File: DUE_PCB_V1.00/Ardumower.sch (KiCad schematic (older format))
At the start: 54 parts, among them J1 9V IN, J10 Sonar_R, J11 Sonar_C, J12 Sonar_L, J13 P_Right, J14 DS3231 RTC, J15 Button, J16 Button, J17 Button, J18 Button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

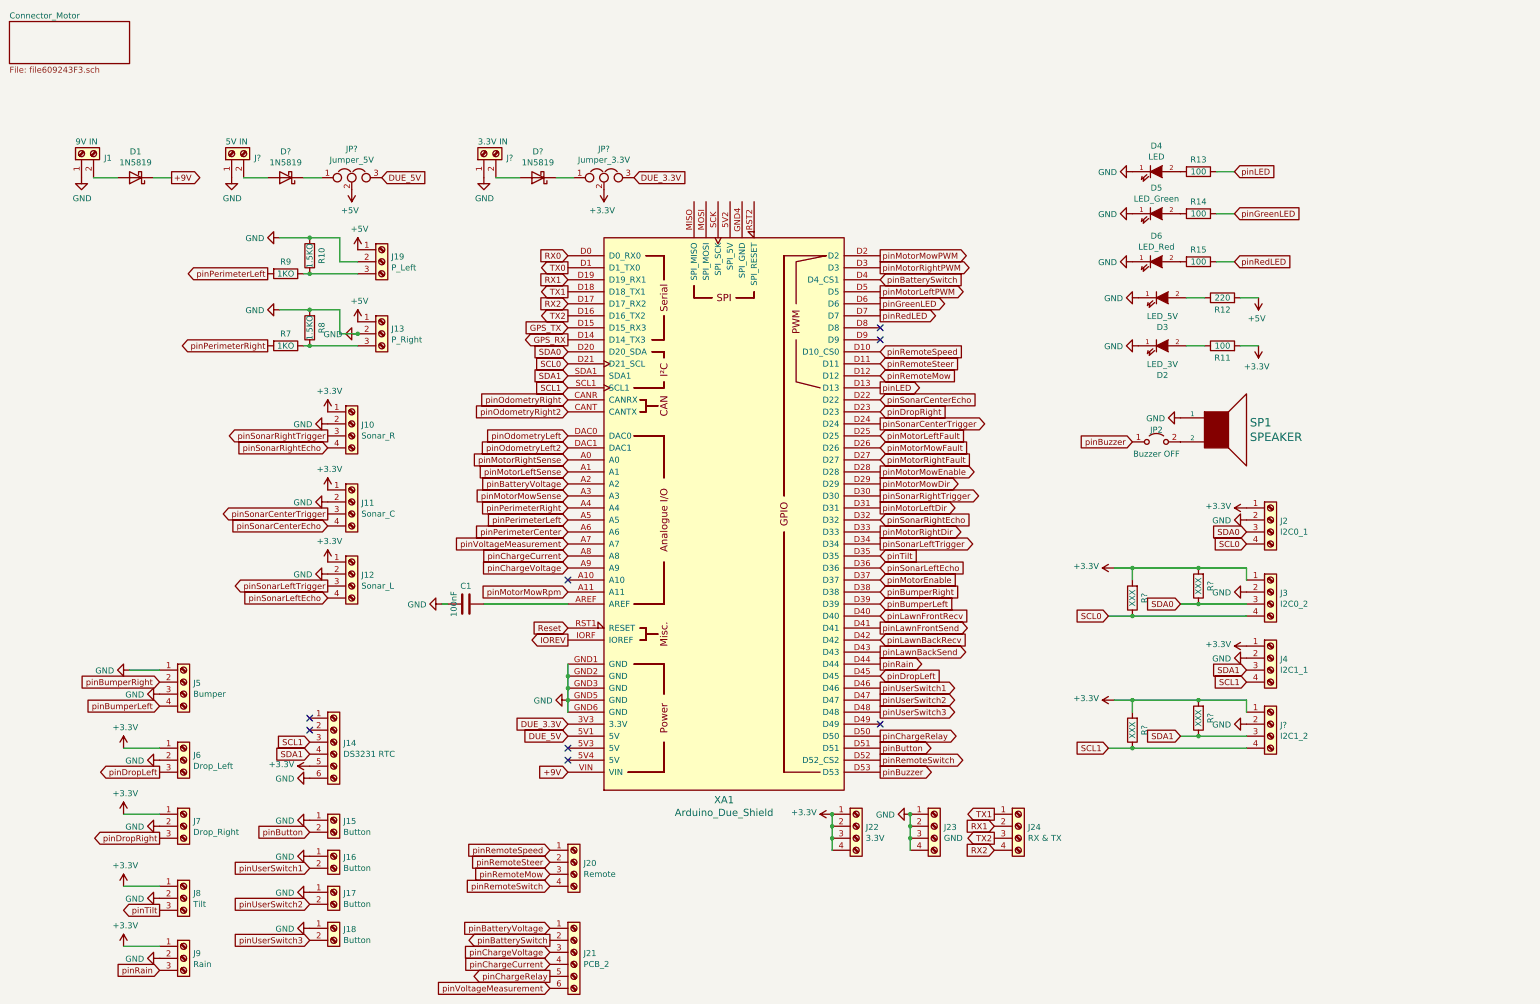
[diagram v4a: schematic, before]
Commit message: Remove RTC Connector
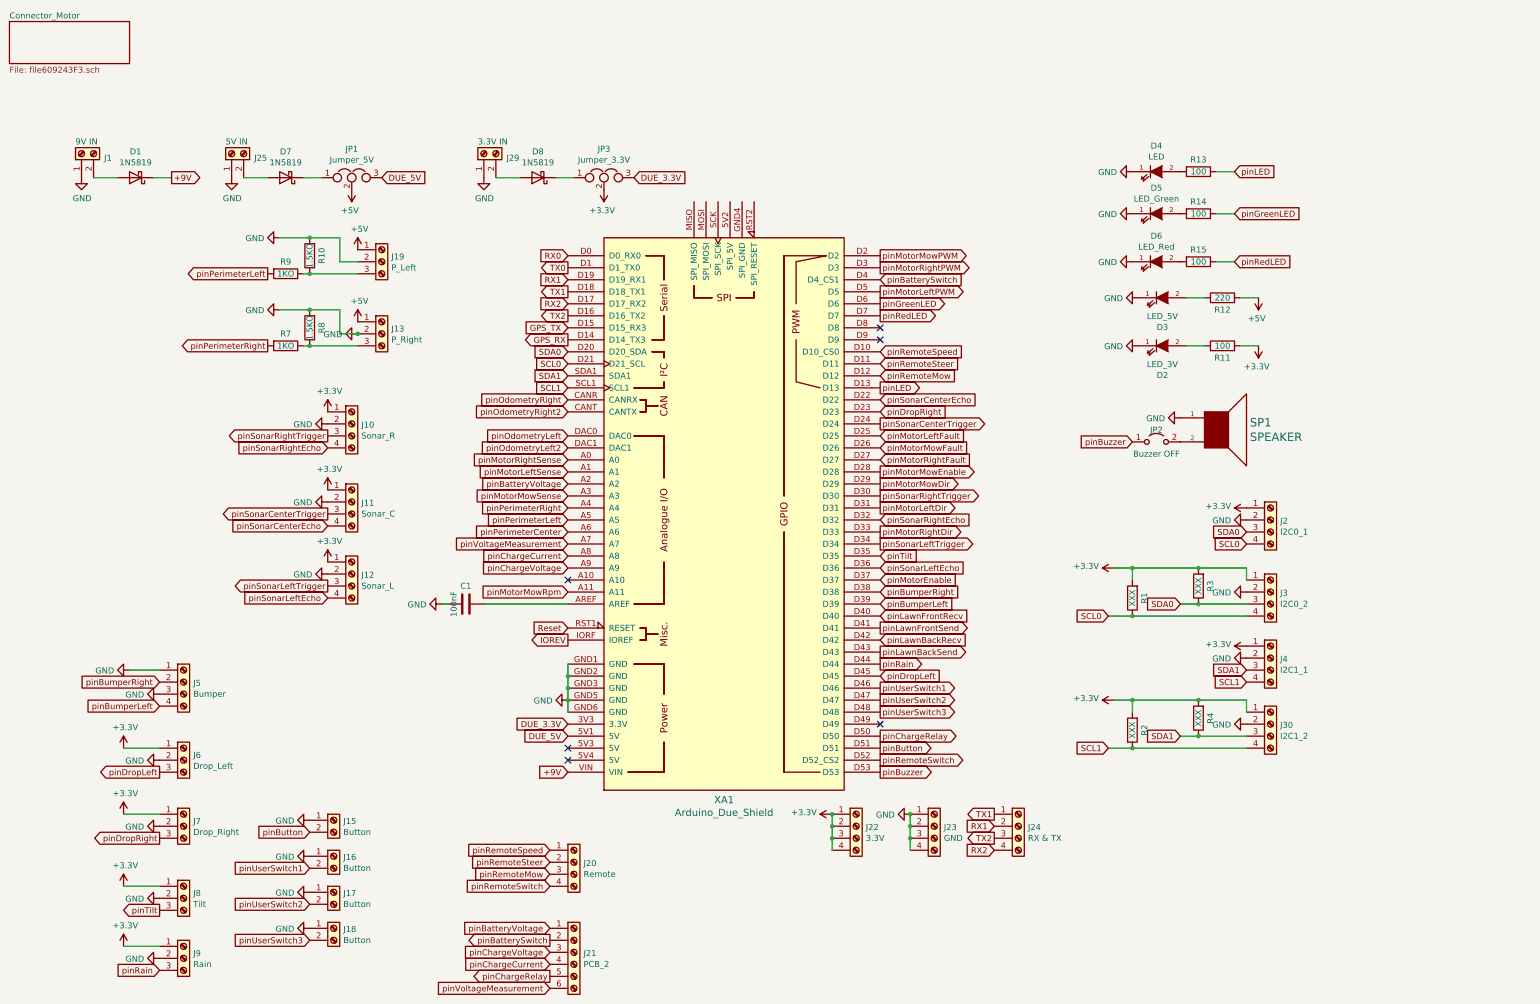
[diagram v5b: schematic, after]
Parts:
- removed J14: DS3231 RTC, Connector_PinHeader_2.54mm:PinHeader_1x06_P2.54mm_Vertical, symbol Connector:Screw_Terminal_01x06
- JP1, JP3: renamed from JP?; footprint (none) -> Connector_PinSocket_2.54mm:PinSocket_1x03_P2.54mm_Vertical
- JP2: footprint Connector_PinHeader_2.54mm:PinHeader_1x02_P2.54mm_Vertical -> Connector_PinSocket_2.54mm:PinSocket_1x02_P2.54mm_Vertical
- gave numbers to parts that had none: 9
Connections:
- no-connect marks 8 -> 6
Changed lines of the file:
@@
 TX1
-$Comp
-L Connector:Screw_Terminal_01x06 J14
-U 1 1 608CA2B5
-P 2900 5550
-F 0 "J14" H 2980 5542 50  0000 L CNN
-F 1 "DS3231 RTC" H 2980 5451 50  0000 L CNN
-F 2 "Connector_PinHeader_2.54mm:PinHeader_1x06_P2.54mm_Vertical" H 2900 5550 50  0001 C CNN
-F 3 "~" H 2900 5550 50  0001 C CNN
-	1    2900 5550
-	1    0    0    -1
-$EndComp
-$Comp
-L power:GND #PWR029
-U 1 1 608CBE4F
-P 2700 5850
-F 0 "#PWR029" H 2700 5600 50  0001 C CNN
-F 1 "GND" V 2705 5722 50  0000 R CNN
-F 2 "" H 2700 5850 50  0001 C CNN
-F 3 "" H 2700 5850 50  0001 C CNN
-	1    2700 5850
-	0    1    1    0
-$EndComp
-$Comp
-L power:+3.3V #PWR028
-U 1 1 608D45C8
-P 2700 5750
-F 0 "#PWR028" H 2700 5600 50  0001 C CNN
-F 1 "+3.3V" V 2715 5878 50  0000 L CNN
-F 2 "" H 2700 5750 50  0001 C CNN
-F 3 "" H 2700 5750 50  0001 C CNN
-	1    2700 5750
-	0    -1   -1   0
-$EndComp
-Text GLabel 2700 5650 0    50   Input ~ 0
-SDA1
-Text GLabel 2700 5550 0    50   Input ~ 0
-SCL1
-NoConn ~ 2700 5450
-NoConn ~ 2700 5350
 $Comp
 L Connector:Screw_Terminal_01x04 J22
@@
 	1400 850  1550 850
 $Comp
-L Connector:Screw_Terminal_01x02 J?
+L Connector:Screw_Terminal_01x02 J25
 U 1 1 60C7263B
 P 2050 650
-F 0 "J?" V 2014 462 50  0000 R CNN
+F 0 "J25" V 2014 462 50  0000 R CNN
 F 1 "5V IN" V 2150 700 50  0000 R CNN
 F 2 "TerminalBlock:TerminalBlock_bornier-2_P5.08mm" H 2050 650 50  0001 C CNN
@@
 $EndComp
 $Comp
-L Diode:1N5819 D?
+L Diode:1N5819 D7
 U 1 1 60C72F7B
 P 2500 850
-F 0 "D?" H 2500 633 50  0000 C CNN
+F 0 "D7" H 2500 633 50  0000 C CNN
 F 1 "1N5819" H 2500 724 50  0000 C CNN
 F 2 "Diode_THT:D_DO-41_SOD81_P10.16mm_Horizontal" H 2500 675 50  0001 C CNN
@@
 $EndComp
 $Comp
-L power:GND #PWR?
+L power:GND #PWR023
 U 1 1 60C72F86
 P 2050 850
-F 0 "#PWR?" H 2050 600 50  0001 C CNN
+F 0 "#PWR023" H 2050 600 50  0001 C CNN
 F 1 "GND" H 2055 677 50  0000 C CNN
 F 2 "" H 2050 850 50  0001 C CNN
@@
 	2650 850  2800 850
 $Comp
-L Connector:Screw_Terminal_01x02 J?
+L Connector:Screw_Terminal_01x02 J29
 U 1 1 60C78D92
 P 4150 650
-F 0 "J?" V 4114 462 50  0000 R CNN
+F 0 "J29" V 4114 462 50  0000 R CNN
 F 1 "3.3V IN" V 4250 700 50  0000 R CNN
 F 2 "TerminalBlock:TerminalBlock_bornier-2_P5.08mm" H 4150 650 50  0001 C CNN
@@
 $EndComp
 $Comp
-L Diode:1N5819 D?
+L Diode:1N5819 D8
 U 1 1 60C7971C
 P 4600 850
-F 0 "D?" H 4600 633 50  0000 C CNN
+F 0 "D8" H 4600 633 50  0000 C CNN
 F 1 "1N5819" H 4600 724 50  0000 C CNN
 F 2 "Diode_THT:D_DO-41_SOD81_P10.16mm_Horizontal" H 4600 675 50  0001 C CNN
@@
 $EndComp
 $Comp
-L power:GND #PWR?
+L power:GND #PWR049
 U 1 1 60C79727
 P 4150 850
-F 0 "#PWR?" H 4150 600 50  0001 C CNN
+F 0 "#PWR049" H 4150 600 50  0001 C CNN
 F 1 "GND" H 4155 677 50  0000 C CNN
 F 2 "" H 4150 850 50  0001 C CNN
@@
 	4750 850  4900 850
 $Comp
-L Device:Jumper_NC_Dual JP?
+L Device:Jumper_NC_Dual JP1
 U 1 1 60C84382
 P 3050 850
-F 0 "JP?" H 3050 1089 50  0000 C CNN
+F 0 "JP1" H 3050 1089 50  0000 C CNN
 F 1 "Jumper_5V" H 3050 998 50  0000 C CNN
-F 2 "" H 3050 850 50  0001 C CNN
+F 2 "Connector_PinSocket_2.54mm:PinSocket_1x03_P2.54mm_Vertical" H 3050 850 50  0001 C CNN
 F 3 "~" H 3050 850 50  0001 C CNN
 	1    3050 850
@@
 DUE_5V
 $Comp
-L power:+5V #PWR?
+L power:+5V #PWR039
 U 1 1 60C8C573
 P 3050 950
-F 0 "#PWR?" H 3050 800 50  0001 C CNN
+F 0 "#PWR039" H 3050 800 50  0001 C CNN
 F 1 "+5V" H 3065 1123 50  0000 C CNN
 F 2 "" H 3050 950 50  0001 C CNN
@@
 $EndComp
 $Comp
-L Device:Jumper_NC_Dual JP?
+L Device:Jumper_NC_Dual JP3
 U 1 1 60C94A1D
 P 5150 850
-F 0 "JP?" H 5150 1089 50  0000 C CNN
+F 0 "JP3" H 5150 1089 50  0000 C CNN
 F 1 "Jumper_3.3V" H 5150 998 50  0000 C CNN
-F 2 "" H 5150 850 50  0001 C CNN
+F 2 "Connector_PinSocket_2.54mm:PinSocket_1x03_P2.54mm_Vertical" H 5150 850 50  0001 C CNN
 F 3 "~" H 5150 850 50  0001 C CNN
 	1    5150 850
@@
 DUE_3.3V
 $Comp
-L power:+3.3V #PWR?
+L power:+3.3V #PWR050
 U 1 1 60C9BB63
 P 5150 950
-F 0 "#PWR?" H 5150 800 50  0001 C CNN
+F 0 "#PWR050" H 5150 800 50  0001 C CNN
 F 1 "+3.3V" H 5165 1123 50  0000 C CNN
 F 2 "" H 5150 950 50  0001 C CNN
@@
 F 0 "JP2" H 9750 3150 50  0000 C CNN
 F 1 "Buzzer OFF" H 9750 2950 50  0000 C CNN
-F 2 "Connector_PinHeader_2.54mm:PinHeader_1x02_P2.54mm_Vertical" H 9750 3050 50  0001 C CNN
+F 2 "Connector_PinSocket_2.54mm:PinSocket_1x02_P2.54mm_Vertical" H 9750 3050 50  0001 C CNN
 F 3 "~" H 9750 3050 50  0001 C CNN
 	1    9750 3050
@@
 $EndComp
 $Comp
-L power:+3.3V #PWR?
+L power:+3.3V #PWR024
 U 1 1 60CD5141
 P 2850 2800
-F 0 "#PWR?" H 2850 2650 50  0001 C CNN
+F 0 "#PWR024" H 2850 2650 50  0001 C CNN
 F 1 "+3.3V" H 2865 2973 50  0000 C CNN
 F 2 "" H 2850 2800 50  0001 C CNN
@@
 $EndComp
 $Comp
-L power:+3.3V #PWR?
+L power:+3.3V #PWR025
 U 1 1 60CD78FD
 P 2850 3450
-F 0 "#PWR?" H 2850 3300 50  0001 C CNN
+F 0 "#PWR025" H 2850 3300 50  0001 C CNN
 F 1 "+3.3V" H 2865 3623 50  0000 C CNN
 F 2 "" H 2850 3450 50  0001 C CNN
@@
 $EndComp
 $Comp
-L power:+3.3V #PWR?
+L power:+3.3V #PWR038
 U 1 1 60CDB03B
 P 2850 4050
-F 0 "#PWR?" H 2850 3900 50  0001 C CNN
+F 0 "#PWR038" H 2850 3900 50  0001 C CNN
 F 1 "+3.3V" H 2865 4223 50  0000 C CNN
 F 2 "" H 2850 4050 50  0001 C CNN
@@
 $EndComp
 $Comp
-L Device:R R?
+L Device:R R3
 U 1 1 60CF47C8
 P 10100 4250
-F 0 "R?" V 10000 4250 50  0000 C CNN
+F 0 "R3" V 10000 4250 50  0000 C CNN
 F 1 "XXX" V 10100 4250 50  0000 C CNN
 F 2 "Resistor_THT:R_Axial_DIN0207_L6.3mm_D2.5mm_P2.54mm_Vertical" V 10030 4250 50  0001 C CNN
@@
 $EndComp
 $Comp
-L Device:R R?
+L Device:R R1
 U 1 1 60CF84E0
 P 9550 4350
-F 0 "R?" V 9450 4350 50  0000 C CNN
+F 0 "R1" V 9450 4350 50  0000 C CNN
 F 1 "XXX" V 9550 4350 50  0000 C CNN
 F 2 "Resistor_THT:R_Axial_DIN0207_L6.3mm_D2.5mm_P2.54mm_Vertical" V 9480 4350 50  0001 C CNN
@@
 	9550 4100 9400 4100
 $Comp
-L Connector:Screw_Terminal_01x04 J?
+L Connector:Screw_Terminal_01x04 J30
 U 1 1 60D185B1
 P 10700 5400
-F 0 "J?" H 10780 5392 50  0000 L CNN
+F 0 "J30" H 10780 5392 50  0000 L CNN
 F 1 "I2C1_2" H 10780 5301 50  0000 L CNN
 F 2 "Connector_PinHeader_2.54mm:PinHeader_1x04_P2.54mm_Vertical" H 10700 5400 50  0001 C CNN
@@
 SCL1
 $Comp
-L power:GND #PWR?
+L power:GND #PWR068
 U 1 1 60D18FDB
 P 10500 5400
-F 0 "#PWR?" H 10500 5150 50  0001 C CNN
+F 0 "#PWR068" H 10500 5150 50  0001 C CNN
 F 1 "GND" V 10505 5272 50  0000 R CNN
 F 2 "" H 10500 5400 50  0001 C CNN
@@
 $EndComp
 $Comp
-L power:+3.3V #PWR?
+L power:+3.3V #PWR051
 U 1 1 60D18FE5
 P 9400 5200
-F 0 "#PWR?" H 9400 5050 50  0001 C CNN
+F 0 "#PWR051" H 9400 5050 50  0001 C CNN
 F 1 "+3.3V" V 9415 5328 50  0000 L CNN
 F 2 "" H 9400 5200 50  0001 C CNN
@@
 $EndComp
 $Comp
-L Device:R R?
+L Device:R R4
 U 1 1 60D18FEF
 P 10100 5350
-F 0 "R?" V 10000 5350 50  0000 C CNN
+F 0 "R4" V 10000 5350 50  0000 C CNN
 F 1 "XXX" V 10100 5350 50  0000 C CNN
 F 2 "Resistor_THT:R_Axial_DIN0207_L6.3mm_D2.5mm_P2.54mm_Vertical" V 10030 5350 50  0001 C CNN
@@
 $EndComp
 $Comp
-L Device:R R?
+L Device:R R2
 U 1 1 60D18FF9
 P 9550 5450
-F 0 "R?" V 9450 5450 50  0000 C CNN
+F 0 "R2" V 9450 5450 50  0000 C CNN
 F 1 "XXX" V 9550 5450 50  0000 C CNN
 F 2 "Resistor_THT:R_Axial_DIN0207_L6.3mm_D2.5mm_P2.54mm_Vertical" V 9480 5450 50  0001 C CNN

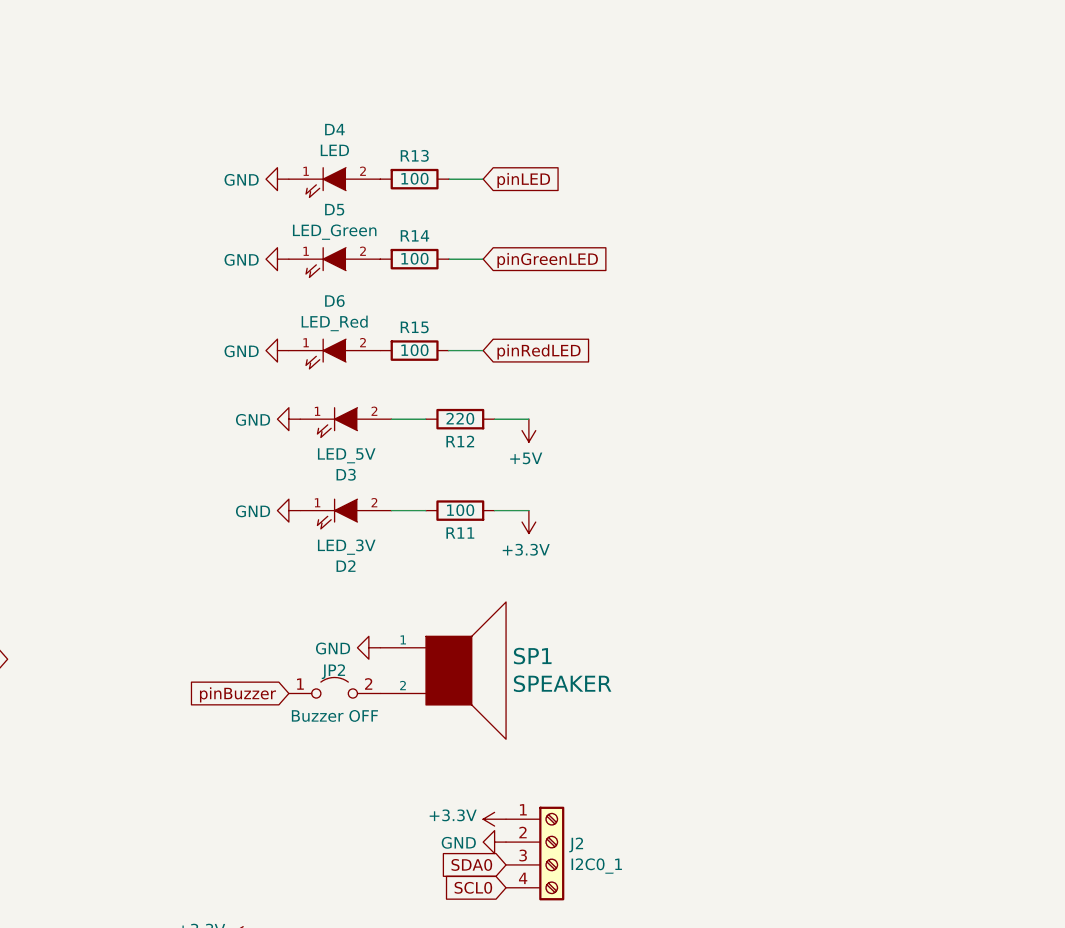
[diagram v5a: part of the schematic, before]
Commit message: Add Mounting Hole
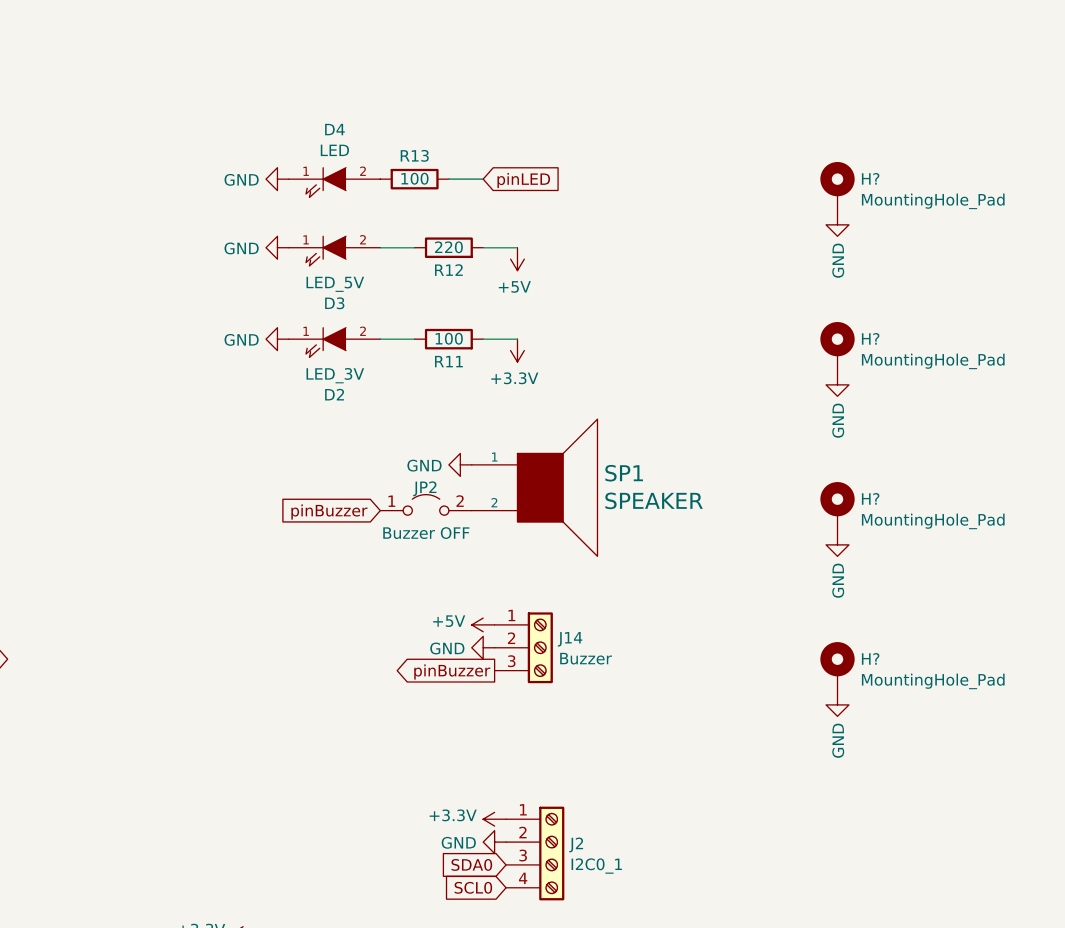
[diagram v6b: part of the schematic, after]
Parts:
- removed D5: LED_Green, LED_THT:LED_D3.0mm, symbol Zimprich:LED
- removed D6: LED_Red, LED_THT:LED_D3.0mm, symbol Zimprich:LED
- removed R14, R15: 100, Resistor_THT:R_Axial_DIN0207_L6.3mm_D2.5mm_P2.54mm_Vertical, symbol Device:R
- added H? (x4): MountingHole_Pad, MountingHole:MountingHole_2.2mm_M2_Pad_TopBottom, symbol Mechanical:MountingHole_Pad
- added J14: Buzzer, Connector_PinHeader_2.54mm:PinHeader_1x03_P2.54mm_Vertical, symbol Connector:Screw_Terminal_01x03
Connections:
- net +5V: now also J14.1 (Pin_1)
- net GND: now also H?.1, H?.1, H?.1, H?.1, J14.2 (Pin_2)
- net pinBuzzer: now also J14.3 (Pin_3)
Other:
- moved on the sheet: D2, D3, JP2, R11, R12, SP1

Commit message: Rename GPS_TX & GPS_RX to RX3 & TX3
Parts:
- gave numbers to parts that had none: 4
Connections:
- net GPS_RX renamed RX3
- net GPS_TX renamed TX3
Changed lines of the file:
@@
 TX2
 Text GLabel 4850 2100 0    50   Input ~ 0
-GPS_TX
+TX3
 Text GLabel 4850 2200 0    50   Output ~ 0
-GPS_RX
+RX3
 Text GLabel 4850 2300 0    50   Input ~ 0
 SDA0
@@
 $EndComp
 $Comp
-L Mechanical:MountingHole_Pad H?
+L Mechanical:MountingHole_Pad H1
 U 1 1 60D6858C
 P 11950 850
-F 0 "H?" H 12050 899 50  0000 L CNN
+F 0 "H1" H 12050 899 50  0000 L CNN
 F 1 "MountingHole_Pad" H 12050 808 50  0000 L CNN
 F 2 "MountingHole:MountingHole_2.2mm_M2_Pad_TopBottom" H 11950 850 50  0001 C CNN
@@
 $EndComp
 $Comp
-L power:GND #PWR?
+L power:GND #PWR047
 U 1 1 60D69D5C
 P 11950 950
-F 0 "#PWR?" H 11950 700 50  0001 C CNN
+F 0 "#PWR047" H 11950 700 50  0001 C CNN
 F 1 "GND" V 11955 822 50  0000 R CNN
 F 2 "" H 11950 950 50  0001 C CNN
@@
 $EndComp
 $Comp
-L Mechanical:MountingHole_Pad H?
+L Mechanical:MountingHole_Pad H2
 U 1 1 60D6E833
 P 11950 1550
-F 0 "H?" H 12050 1599 50  0000 L CNN
+F 0 "H2" H 12050 1599 50  0000 L CNN
 F 1 "MountingHole_Pad" H 12050 1508 50  0000 L CNN
 F 2 "MountingHole:MountingHole_2.2mm_M2_Pad_TopBottom" H 11950 1550 50  0001 C CNN
@@
 $EndComp
 $Comp
-L power:GND #PWR?
+L power:GND #PWR048
 U 1 1 60D6F1F9
 P 11950 1650
-F 0 "#PWR?" H 11950 1400 50  0001 C CNN
+F 0 "#PWR048" H 11950 1400 50  0001 C CNN
 F 1 "GND" V 11955 1522 50  0000 R CNN
 F 2 "" H 11950 1650 50  0001 C CNN
@@
 $EndComp
 $Comp
-L Mechanical:MountingHole_Pad H?
+L Mechanical:MountingHole_Pad H3
 U 1 1 60D7064F
 P 11950 2250
-F 0 "H?" H 12050 2299 50  0000 L CNN
+F 0 "H3" H 12050 2299 50  0000 L CNN
 F 1 "MountingHole_Pad" H 12050 2208 50  0000 L CNN
 F 2 "MountingHole:MountingHole_2.2mm_M2_Pad_TopBottom" H 11950 2250 50  0001 C CNN
@@
 $EndComp
 $Comp
-L power:GND #PWR?
+L power:GND #PWR069
 U 1 1 60D7102F
 P 11950 2350
-F 0 "#PWR?" H 11950 2100 50  0001 C CNN
+F 0 "#PWR069" H 11950 2100 50  0001 C CNN
 F 1 "GND" V 11955 2222 50  0000 R CNN
 F 2 "" H 11950 2350 50  0001 C CNN
@@
 $EndComp
 $Comp
-L Mechanical:MountingHole_Pad H?
+L Mechanical:MountingHole_Pad H4
 U 1 1 60D71039
 P 11950 2950
-F 0 "H?" H 12050 2999 50  0000 L CNN
+F 0 "H4" H 12050 2999 50  0000 L CNN
 F 1 "MountingHole_Pad" H 12050 2908 50  0000 L CNN
 F 2 "MountingHole:MountingHole_2.2mm_M2_Pad_TopBottom" H 11950 2950 50  0001 C CNN
@@
 $EndComp
 $Comp
-L power:GND #PWR?
+L power:GND #PWR070
 U 1 1 60D71043
 P 11950 3050
-F 0 "#PWR?" H 11950 2800 50  0001 C CNN
+F 0 "#PWR070" H 11950 2800 50  0001 C CNN
 F 1 "GND" V 11955 2922 50  0000 R CNN
 F 2 "" H 11950 3050 50  0001 C CNN
